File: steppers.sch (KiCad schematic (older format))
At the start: 24 parts, among them J1 HEADER, J10 STEPSTICK, J11 STEPSTICK, J12 STEPSTICK, J2 HEADER, J3 HEADER, J4 STEPSTICK, J5 STEPSTICK, J6 STEPSTICK, J7 HEADER, J8 HEADER, J9 HEADER, P10 CONN_01X04, P11 CONN_01X04, P12 CONN_01X04, P7 CONN_01X04, P8 CONN_01X04, P9 CONN_01X04

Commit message: more schematics
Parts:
- C12, C13, C14, C15, C16, C17: footprint (none) -> geda-footprints:ELCO-8mm
- J1, J2, J3, J7, J8, J9: footprint (none) -> geda-footprints:CON_HDR_2x3
- J10, J11, J12, J4, J5, J6: footprint (none) -> geda-footprints:STEPSTICK
- P10, P11, P12, P7, P8, P9: footprint (none) -> geda-footprints:CON_HDR_1x4
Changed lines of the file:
@@
 F 0 "J5" H 2475 2750 34  0000 C CNN
 F 1 "STEPSTICK" H 2475 2650 34  0000 C CNN
-F 2 "" H 2025 1925 60  0001 C CNN
+F 2 "geda-footprints:STEPSTICK" H 2025 1925 60  0001 C CNN
 F 3 "" H 2025 1925 60  0000 C CNN
 	1    2025 1925
@@
 F 0 "C13" H 3888 1471 50  0000 L CNN
 F 1 "100uF" H 3888 1379 50  0000 L CNN
-F 2 "" H 3800 1425 50  0001 C CNN
+F 2 "geda-footprints:ELCO-8mm" H 3800 1425 50  0001 C CNN
 F 3 "" H 3800 1425 50  0000 C CNN
 	1    3800 1425
@@
 F 0 "J2" H 1325 1907 34  0000 C CNN
 F 1 "HEADER" H 1325 1838 34  0000 C CNN
-F 2 "" H 1150 1475 60  0001 C CNN
+F 2 "geda-footprints:CON_HDR_2x3" H 1150 1475 60  0001 C CNN
 F 3 "" H 1150 1475 60  0000 C CNN
 	1    1150 1475
@@
 F 0 "P8" H 3477 1513 50  0000 L CNN
 F 1 "CONN_01X04" H 3477 1421 50  0000 L CNN
-F 2 "" H 3400 1475 50  0001 C CNN
+F 2 "geda-footprints:CON_HDR_1x4" H 3400 1475 50  0001 C CNN
 F 3 "" H 3400 1475 50  0000 C CNN
 	1    3400 1475
@@
 F 0 "J6" H 2475 3975 34  0000 C CNN
 F 1 "STEPSTICK" H 2475 3875 34  0000 C CNN
-F 2 "" H 2025 3150 60  0001 C CNN
+F 2 "geda-footprints:STEPSTICK" H 2025 3150 60  0001 C CNN
 F 3 "" H 2025 3150 60  0000 C CNN
 	1    2025 3150
@@
 F 0 "C14" H 3888 2696 50  0000 L CNN
 F 1 "100uF" H 3888 2604 50  0000 L CNN
-F 2 "" H 3800 2650 50  0001 C CNN
+F 2 "geda-footprints:ELCO-8mm" H 3800 2650 50  0001 C CNN
 F 3 "" H 3800 2650 50  0000 C CNN
 	1    3800 2650
@@
 F 0 "J3" H 1325 3132 34  0000 C CNN
 F 1 "HEADER" H 1325 3063 34  0000 C CNN
-F 2 "" H 1150 2700 60  0001 C CNN
+F 2 "geda-footprints:CON_HDR_2x3" H 1150 2700 60  0001 C CNN
 F 3 "" H 1150 2700 60  0000 C CNN
 	1    1150 2700
@@
 F 0 "P9" H 3477 2738 50  0000 L CNN
 F 1 "CONN_01X04" H 3477 2646 50  0000 L CNN
-F 2 "" H 3400 2700 50  0001 C CNN
+F 2 "geda-footprints:CON_HDR_1x4" H 3400 2700 50  0001 C CNN
 F 3 "" H 3400 2700 50  0000 C CNN
 	1    3400 2700
@@
 F 0 "J4" H 2450 5275 34  0000 C CNN
 F 1 "STEPSTICK" H 2450 5175 34  0000 C CNN
-F 2 "" H 2000 4450 60  0001 C CNN
+F 2 "geda-footprints:STEPSTICK" H 2000 4450 60  0001 C CNN
 F 3 "" H 2000 4450 60  0000 C CNN
 	1    2000 4450
@@
 F 0 "C12" H 3863 3996 50  0000 L CNN
 F 1 "100uF" H 3863 3904 50  0000 L CNN
-F 2 "" H 3775 3950 50  0001 C CNN
+F 2 "geda-footprints:ELCO-8mm" H 3775 3950 50  0001 C CNN
 F 3 "" H 3775 3950 50  0000 C CNN
 	1    3775 3950
@@
 F 0 "J1" H 1300 4432 34  0000 C CNN
 F 1 "HEADER" H 1300 4363 34  0000 C CNN
-F 2 "" H 1125 4000 60  0001 C CNN
+F 2 "geda-footprints:CON_HDR_2x3" H 1125 4000 60  0001 C CNN
 F 3 "" H 1125 4000 60  0000 C CNN
 	1    1125 4000
@@
 F 0 "P7" H 3452 4038 50  0000 L CNN
 F 1 "CONN_01X04" H 3452 3946 50  0000 L CNN
-F 2 "" H 3375 4000 50  0001 C CNN
+F 2 "geda-footprints:CON_HDR_1x4" H 3375 4000 50  0001 C CNN
 F 3 "" H 3375 4000 50  0000 C CNN
 	1    3375 4000
@@
 F 0 "J10" H 7625 2775 34  0000 C CNN
 F 1 "STEPSTICK" H 7625 2675 34  0000 C CNN
-F 2 "" H 7175 1950 60  0001 C CNN
+F 2 "geda-footprints:STEPSTICK" H 7175 1950 60  0001 C CNN
 F 3 "" H 7175 1950 60  0000 C CNN
 	1    7175 1950
@@
 F 0 "C15" H 9038 1496 50  0000 L CNN
 F 1 "100uF" H 9038 1404 50  0000 L CNN
-F 2 "" H 8950 1450 50  0001 C CNN
+F 2 "geda-footprints:ELCO-8mm" H 8950 1450 50  0001 C CNN
 F 3 "" H 8950 1450 50  0000 C CNN
 	1    8950 1450
@@
 F 0 "J7" H 6475 1932 34  0000 C CNN
 F 1 "HEADER" H 6475 1863 34  0000 C CNN
-F 2 "" H 6300 1500 60  0001 C CNN
+F 2 "geda-footprints:CON_HDR_2x3" H 6300 1500 60  0001 C CNN
 F 3 "" H 6300 1500 60  0000 C CNN
 	1    6300 1500
@@
 F 0 "P10" H 8627 1538 50  0000 L CNN
 F 1 "CONN_01X04" H 8627 1446 50  0000 L CNN
-F 2 "" H 8550 1500 50  0001 C CNN
+F 2 "geda-footprints:CON_HDR_1x4" H 8550 1500 50  0001 C CNN
 F 3 "" H 8550 1500 50  0000 C CNN
 	1    8550 1500
@@
 F 0 "J11" H 7650 4150 34  0000 C CNN
 F 1 "STEPSTICK" H 7650 4050 34  0000 C CNN
-F 2 "" H 7200 3325 60  0001 C CNN
+F 2 "geda-footprints:STEPSTICK" H 7200 3325 60  0001 C CNN
 F 3 "" H 7200 3325 60  0000 C CNN
 	1    7200 3325
@@
 F 0 "C16" H 9063 2871 50  0000 L CNN
 F 1 "100uF" H 9063 2779 50  0000 L CNN
-F 2 "" H 8975 2825 50  0001 C CNN
+F 2 "geda-footprints:ELCO-8mm" H 8975 2825 50  0001 C CNN
 F 3 "" H 8975 2825 50  0000 C CNN
 	1    8975 2825
@@
 F 0 "J8" H 6500 3307 34  0000 C CNN
 F 1 "HEADER" H 6500 3238 34  0000 C CNN
-F 2 "" H 6325 2875 60  0001 C CNN
+F 2 "geda-footprints:CON_HDR_2x3" H 6325 2875 60  0001 C CNN
 F 3 "" H 6325 2875 60  0000 C CNN
 	1    6325 2875
@@
 F 0 "P11" H 8652 2913 50  0000 L CNN
 F 1 "CONN_01X04" H 8652 2821 50  0000 L CNN
-F 2 "" H 8575 2875 50  0001 C CNN
+F 2 "geda-footprints:CON_HDR_1x4" H 8575 2875 50  0001 C CNN
 F 3 "" H 8575 2875 50  0000 C CNN
 	1    8575 2875
@@
 F 0 "J12" H 7650 5525 34  0000 C CNN
 F 1 "STEPSTICK" H 7650 5425 34  0000 C CNN
-F 2 "" H 7200 4700 60  0001 C CNN
+F 2 "geda-footprints:STEPSTICK" H 7200 4700 60  0001 C CNN
 F 3 "" H 7200 4700 60  0000 C CNN
 	1    7200 4700
@@
 F 0 "C17" H 9063 4246 50  0000 L CNN
 F 1 "100uF" H 9063 4154 50  0000 L CNN
-F 2 "" H 8975 4200 50  0001 C CNN
+F 2 "geda-footprints:ELCO-8mm" H 8975 4200 50  0001 C CNN
 F 3 "" H 8975 4200 50  0000 C CNN
 	1    8975 4200
@@
 F 0 "J9" H 6500 4682 34  0000 C CNN
 F 1 "HEADER" H 6500 4613 34  0000 C CNN
-F 2 "" H 6325 4250 60  0001 C CNN
+F 2 "geda-footprints:CON_HDR_2x3" H 6325 4250 60  0001 C CNN
 F 3 "" H 6325 4250 60  0000 C CNN
 	1    6325 4250
@@
 F 0 "P12" H 8652 4288 50  0000 L CNN
 F 1 "CONN_01X04" H 8652 4196 50  0000 L CNN
-F 2 "" H 8575 4250 50  0001 C CNN
+F 2 "geda-footprints:CON_HDR_1x4" H 8575 4250 50  0001 C CNN
 F 3 "" H 8575 4250 50  0000 C CNN
 	1    8575 4250

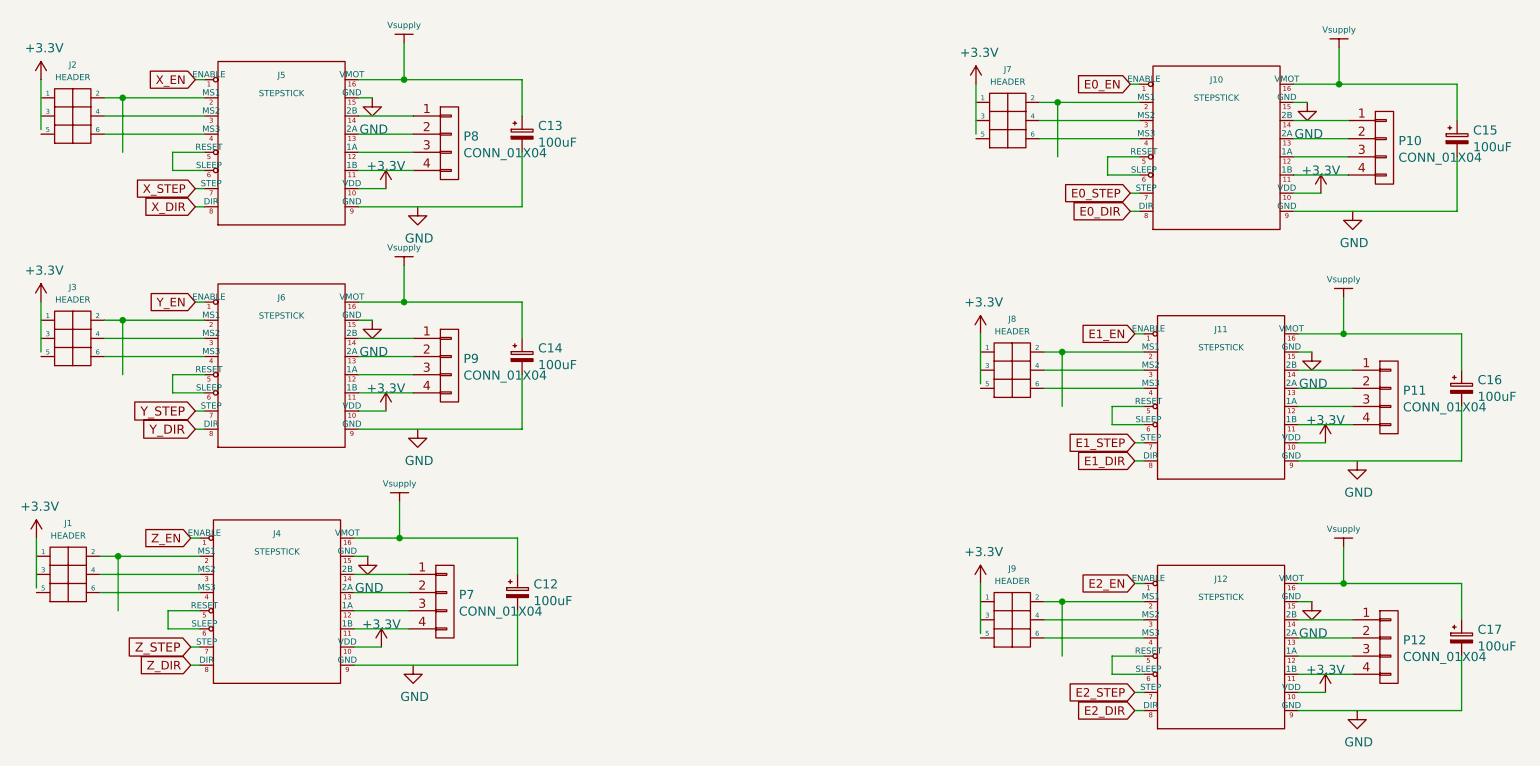
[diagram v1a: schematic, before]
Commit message: more placement and routing
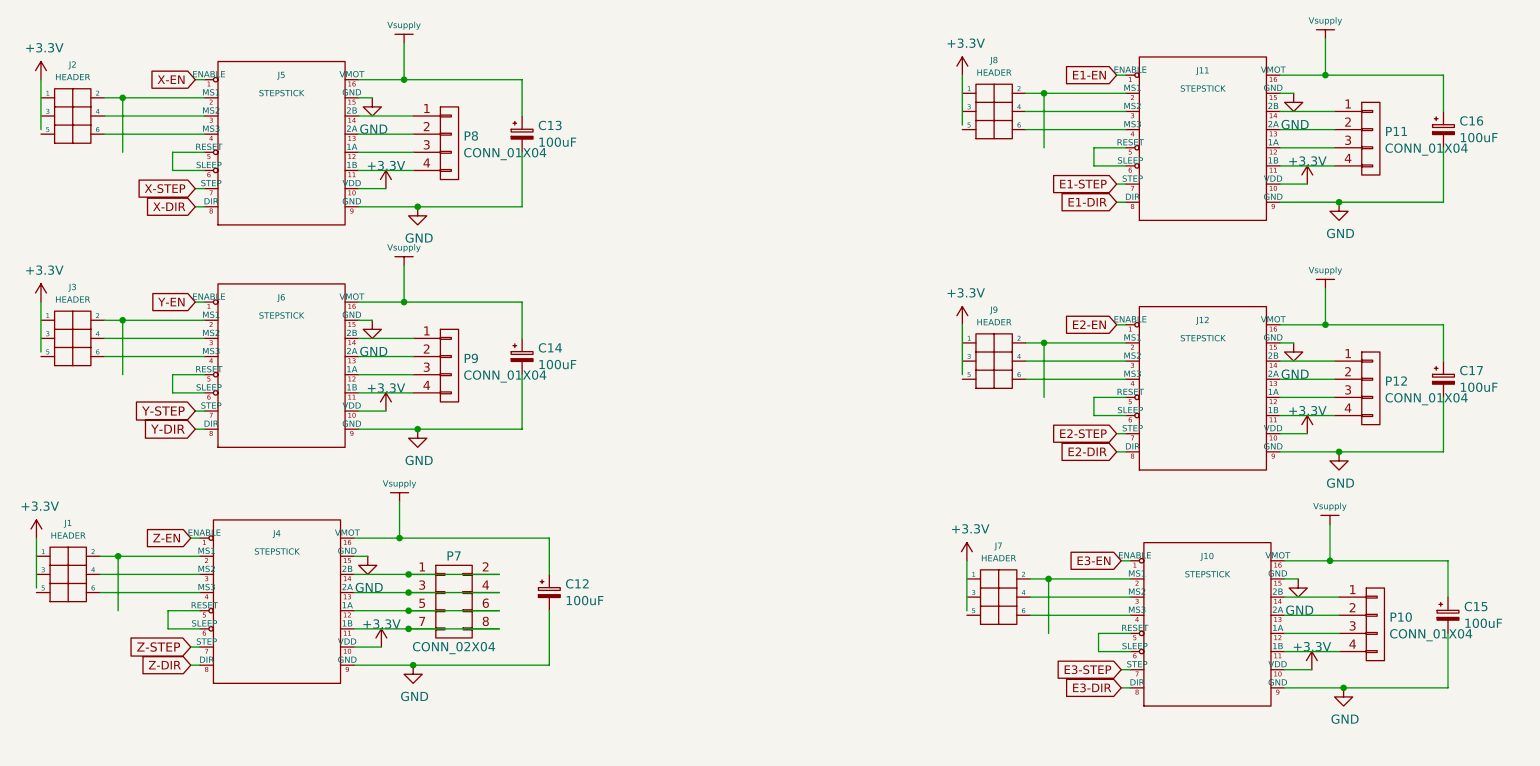
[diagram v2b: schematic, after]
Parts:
- removed P7: CONN_01X04, geda-footprints:CON_HDR_1x4, symbol CONN_01X04
- added P7: CONN_02X04, geda-footprints:CON_HDR_2x4, symbol CONN_02X04
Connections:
- net labels added: E1-DIR, E1-EN, E1-STEP, E2-DIR, E2-EN, E2-STEP, E3-DIR, E3-EN, E3-STEP, X-DIR, X-EN, X-STEP, Y-DIR, Y-EN, Y-STEP, Z-DIR, Z-EN, Z-STEP
- net labels removed: E0_DIR, E0_EN, E0_STEP, E1_DIR, E1_EN, E1_STEP, E2_DIR, E2_EN, E2_STEP, X_DIR, X_EN, X_STEP, Y_DIR, Y_EN, Y_STEP, Z_DIR, Z_EN, Z_STEP
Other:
- moved on the sheet: C12, C15, C16, C17, J10, J11, J12, J7, J8, J9, P10, P11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

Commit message: More routing
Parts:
- C12, C13, C14, C15, C16, C17: footprint geda-footprints:ELCO-8mm -> armin-footprints:ELCO-8mm
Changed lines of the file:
@@
 $EndDescr
 Wire Wire Line
-	3800 1525 3800 1825
-Wire Wire Line
-	3800 1825 2900 1825
+	3800 1825 3800 1525
+Wire Wire Line
+	2900 1825 3800 1825
 Wire Wire Line
 	2050 1825 2000 1825
@@
 F 0 "C13" H 3888 1471 50  0000 L CNN
 F 1 "100uF" H 3888 1379 50  0000 L CNN
-F 2 "geda-footprints:ELCO-8mm" H 3800 1425 50  0001 C CNN
+F 2 "armin-footprints:ELCO-8mm" H 3800 1425 50  0001 C CNN
 F 3 "" H 3800 1425 50  0000 C CNN
 	1    3800 1425
@@
 L HEADER8 J2
 U 1 1 568BF3C9
-P 1150 1475
-F 0 "J2" H 1325 1907 34  0000 C CNN
-F 1 "HEADER" H 1325 1838 34  0000 C CNN
-F 2 "geda-footprints:CON_HDR_2x3" H 1150 1475 60  0001 C CNN
-F 3 "" H 1150 1475 60  0000 C CNN
-	1    1150 1475
-	1    0    0    -1
-$EndComp
-Wire Wire Line
-	1150 1400 1150 1125
+P 1500 1475
+F 0 "J2" H 1675 1907 34  0000 C CNN
+F 1 "HEADER" H 1675 1838 34  0000 C CNN
+F 2 "geda-footprints:CON_HDR_2x3" H 1500 1475 60  0001 C CNN
+F 3 "" H 1500 1475 60  0000 C CNN
+	1    1500 1475
+	-1   0    0    -1
+$EndComp
+Wire Wire Line
+	1150 1125 1150 1425
 $Comp
 L +3.3V #PWR054
@@
 	2975 1225 2900 1225
 Wire Wire Line
-	3800 2750 3800 3050
-Wire Wire Line
-	3800 3050 2900 3050
+	3800 3050 3800 2750
+Wire Wire Line
+	2900 3050 3800 3050
 Wire Wire Line
 	2050 3050 2000 3050
@@
 	2900 2350 3800 2350
 Connection ~ 3150 2350
-Wire Wire Line
-	1600 2450 1600 2750
-Connection ~ 1600 2450
 Text GLabel 2000 2350 0    47   Input ~ 0
 Y-EN
@@
 F 0 "C14" H 3888 2696 50  0000 L CNN
 F 1 "100uF" H 3888 2604 50  0000 L CNN
-F 2 "geda-footprints:ELCO-8mm" H 3800 2650 50  0001 C CNN
+F 2 "armin-footprints:ELCO-8mm" H 3800 2650 50  0001 C CNN
 F 3 "" H 3800 2650 50  0000 C CNN
 	1    3800 2650
@@
 L HEADER8 J3
 U 1 1 568BD85B
-P 1150 2700
-F 0 "J3" H 1325 3132 34  0000 C CNN
-F 1 "HEADER" H 1325 3063 34  0000 C CNN
-F 2 "geda-footprints:CON_HDR_2x3" H 1150 2700 60  0001 C CNN
-F 3 "" H 1150 2700 60  0000 C CNN
-	1    1150 2700
-	1    0    0    -1
-$EndComp
-Wire Wire Line
-	1150 2625 1150 2350
+P 1500 2700
+F 0 "J3" H 1675 3132 34  0000 C CNN
+F 1 "HEADER" H 1675 3063 34  0000 C CNN
+F 2 "geda-footprints:CON_HDR_2x3" H 1500 2700 60  0001 C CNN
+F 3 "" H 1500 2700 60  0000 C CNN
+	1    1500 2700
+	-1   0    0    -1
+$EndComp
+Wire Wire Line
+	1150 2375 1150 2650
 $Comp
 L +3.3V #PWR059
 U 1 1 568BD862
-P 1150 2350
-F 0 "#PWR059" H 1150 2200 50  0001 C CNN
-F 1 "+3.3V" H 1168 2524 50  0000 C CNN
-F 2 "" H 1150 2350 50  0000 C CNN
-F 3 "" H 1150 2350 50  0000 C CNN
-	1    1150 2350
+P 1150 2375
+F 0 "#PWR059" H 1150 2225 50  0001 C CNN
+F 1 "+3.3V" H 1168 2549 50  0000 C CNN
+F 2 "" H 1150 2375 50  0000 C CNN
+F 3 "" H 1150 2375 50  0000 C CNN
+	1    1150 2375
 	1    0    0    -1
 $EndComp
@@
 	2975 2450 2900 2450
 Wire Wire Line
-	3950 4050 3950 4350
-Wire Wire Line
-	3950 4350 2875 4350
+	3950 4350 3950 4050
+Wire Wire Line
+	2875 4350 3950 4350
 Wire Wire Line
 	2025 4350 1975 4350
@@
 F 0 "C12" H 4038 3996 50  0000 L CNN
 F 1 "100uF" H 4038 3904 50  0000 L CNN
-F 2 "geda-footprints:ELCO-8mm" H 3950 3950 50  0001 C CNN
+F 2 "armin-footprints:ELCO-8mm" H 3950 3950 50  0001 C CNN
 F 3 "" H 3950 3950 50  0000 C CNN
 	1    3950 3950
@@
 Wire Wire Line
 	1850 4050 2025 4050
-$Comp
-L HEADER8 J1
-U 1 1 568BDFD4
-P 1125 4000
-F 0 "J1" H 1300 4432 34  0000 C CNN
-F 1 "HEADER" H 1300 4363 34  0000 C CNN
-F 2 "geda-footprints:CON_HDR_2x3" H 1125 4000 60  0001 C CNN
-F 3 "" H 1125 4000 60  0000 C CNN
-	1    1125 4000
-	1    0    0    -1
-$EndComp
-Wire Wire Line
-	1125 3925 1125 3650
+Wire Wire Line
+	1125 3650 1125 3950
 $Comp
 L +3.3V #PWR064
@@
 	2950 3750 2875 3750
 Wire Wire Line
-	8900 4175 8900 4475
-Wire Wire Line
-	8900 4475 8000 4475
+	8900 4475 8900 4175
+Wire Wire Line
+	8000 4475 8900 4475
 Wire Wire Line
 	7150 4475 7100 4475
@@
 F 0 "C15" H 8988 4121 50  0000 L CNN
 F 1 "100uF" H 8988 4029 50  0000 L CNN
-F 2 "geda-footprints:ELCO-8mm" H 8900 4075 50  0001 C CNN
+F 2 "armin-footprints:ELCO-8mm" H 8900 4075 50  0001 C CNN
 F 3 "" H 8900 4075 50  0000 C CNN
 	1    8900 4075
@@
 L HEADER8 J7
 U 1 1 568C3A02
-P 6250 4125
-F 0 "J7" H 6425 4557 34  0000 C CNN
-F 1 "HEADER" H 6425 4488 34  0000 C CNN
-F 2 "geda-footprints:CON_HDR_2x3" H 6250 4125 60  0001 C CNN
-F 3 "" H 6250 4125 60  0000 C CNN
-	1    6250 4125
-	1    0    0    -1
-$EndComp
-Wire Wire Line
-	6250 4050 6250 3775
+P 6600 4125
+F 0 "J7" H 6775 4557 34  0000 C CNN
+F 1 "HEADER" H 6775 4488 34  0000 C CNN
+F 2 "geda-footprints:CON_HDR_2x3" H 6600 4125 60  0001 C CNN
+F 3 "" H 6600 4125 60  0000 C CNN
+	1    6600 4125
+	-1   0    0    -1
+$EndComp
+Wire Wire Line
+	6250 4075 6250 3775
 $Comp
 L +3.3V #PWR069
@@
 	8075 3875 8000 3875
 Wire Wire Line
-	8875 1500 8875 1800
-Wire Wire Line
-	8875 1800 7975 1800
+	8875 1800 8875 1500
+Wire Wire Line
+	7975 1800 8875 1800
 Wire Wire Line
 	7125 1800 7075 1800
@@
 	6675 1200 6675 1500
 Connection ~ 6675 1200
-Text GLabel 7075 1100 0    47   Input ~ 0
+Text GLabel 7075 2475 0    47   Input ~ 0
 E1-EN
-Text GLabel 7075 1800 0    47   Input ~ 0
+Text GLabel 7075 3175 0    47   Input ~ 0
 E1-DIR
-Text GLabel 7075 1700 0    47   Input ~ 0
+Text GLabel 7075 3075 0    47   Input ~ 0
 E1-STEP
 $Comp
@@
 F 0 "C16" H 8963 1446 50  0000 L CNN
 F 1 "100uF" H 8963 1354 50  0000 L CNN
-F 2 "geda-footprints:ELCO-8mm" H 8875 1400 50  0001 C CNN
+F 2 "armin-footprints:ELCO-8mm" H 8875 1400 50  0001 C CNN
 F 3 "" H 8875 1400 50  0000 C CNN
 	1    8875 1400
@@
 L HEADER8 J8
 U 1 1 568C3E66
-P 6225 1450
-F 0 "J8" H 6400 1882 34  0000 C CNN
-F 1 "HEADER" H 6400 1813 34  0000 C CNN
-F 2 "geda-footprints:CON_HDR_2x3" H 6225 1450 60  0001 C CNN
-F 3 "" H 6225 1450 60  0000 C CNN
-	1    6225 1450
-	1    0    0    -1
-$EndComp
-Wire Wire Line
-	6225 1375 6225 1100
+P 6575 1450
+F 0 "J8" H 6750 1882 34  0000 C CNN
+F 1 "HEADER" H 6750 1813 34  0000 C CNN
+F 2 "geda-footprints:CON_HDR_2x3" H 6575 1450 60  0001 C CNN
+F 3 "" H 6575 1450 60  0000 C CNN
+	1    6575 1450
+	-1   0    0    -1
+$EndComp
+Wire Wire Line
+	6225 1100 6225 1400
 $Comp
 L +3.3V #PWR074
@@
 	8050 1200 7975 1200
 Wire Wire Line
-	8875 2875 8875 3175
-Wire Wire Line
-	8875 3175 7975 3175
+	8875 3175 8875 2875
+Wire Wire Line
+	7975 3175 8875 3175
 Wire Wire Line
 	7125 3175 7075 3175
@@
 	6675 2575 6675 2875
 Connection ~ 6675 2575
-Text GLabel 7075 2475 0    47   Input ~ 0
+Text GLabel 7075 1100 0    47   Input ~ 0
 E2-EN
-Text GLabel 7075 3175 0    47   Input ~ 0
+Text GLabel 7075 1800 0    47   Input ~ 0
 E2-DIR
-Text GLabel 7075 3075 0    47   Input ~ 0
+Text GLabel 7075 1700 0    47   Input ~ 0
 E2-STEP
 $Comp
@@
 F 0 "C17" H 8963 2821 50  0000 L CNN
 F 1 "100uF" H 8963 2729 50  0000 L CNN
-F 2 "geda-footprints:ELCO-8mm" H 8875 2775 50  0001 C CNN
+F 2 "armin-footprints:ELCO-8mm" H 8875 2775 50  0001 C CNN
 F 3 "" H 8875 2775 50  0000 C CNN
 	1    8875 2775
@@
 L HEADER8 J9
 U 1 1 568C432F
-P 6225 2825
-F 0 "J9" H 6400 3257 34  0000 C CNN
-F 1 "HEADER" H 6400 3188 34  0000 C CNN
-F 2 "geda-footprints:CON_HDR_2x3" H 6225 2825 60  0001 C CNN
-F 3 "" H 6225 2825 60  0000 C CNN
-	1    6225 2825
-	1    0    0    -1
-$EndComp
-Wire Wire Line
-	6225 2750 6225 2475
+P 6575 2825
+F 0 "J9" H 6750 3257 34  0000 C CNN
+F 1 "HEADER" H 6750 3188 34  0000 C CNN
+F 2 "geda-footprints:CON_HDR_2x3" H 6575 2825 60  0001 C CNN
+F 3 "" H 6575 2825 60  0000 C CNN
+	1    6575 2825
+	-1   0    0    -1
+$EndComp
+Wire Wire Line
+	6225 2475 6225 2775
 $Comp
 L +3.3V #PWR079
@@
 Connection ~ 8300 3175
 Connection ~ 8325 4475
+Connection ~ 1150 2450
+Connection ~ 1150 2550
+Connection ~ 1600 2450
+Wire Wire Line
+	1600 2450 1600 2750
+Connection ~ 1150 1225
+Connection ~ 1150 1325
+$Comp
+L HEADER8 J1
+U 1 1 568BDFD4
+P 1475 4000
+F 0 "J1" H 1650 4432 34  0000 C CNN
+F 1 "HEADER" H 1650 4363 34  0000 C CNN
+F 2 "geda-footprints:CON_HDR_2x3" H 1475 4000 60  0001 C CNN
+F 3 "" H 1475 4000 60  0000 C CNN
+	1    1475 4000
+	-1   0    0    -1
+$EndComp
+Connection ~ 1125 3750
+Connection ~ 1125 3850
+Connection ~ 6225 1200
+Connection ~ 6225 1300
+Connection ~ 6225 2575
+Connection ~ 6225 2675
+Connection ~ 6250 3875
+Connection ~ 6250 3975
 $EndSCHEMATC
